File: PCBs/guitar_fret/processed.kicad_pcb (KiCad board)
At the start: 2 copper layers, 51 parts, among them J1 +5V, J10 CONN_01X06, J11 SWCLK, J2 GNDPWR, J3 +3.3V, J4 GND, J5 SDA, J6 SCL, J7 BOOT0, J8 NRST, J9 SWDIO, P0 TOUCH, P1 TOUCH, P2 TOUCH, P3 TOUCH, P4 TOUCH, P5 TOUCH, U1 STM32F051K*T, U2 AP2210N-3.3TRG1

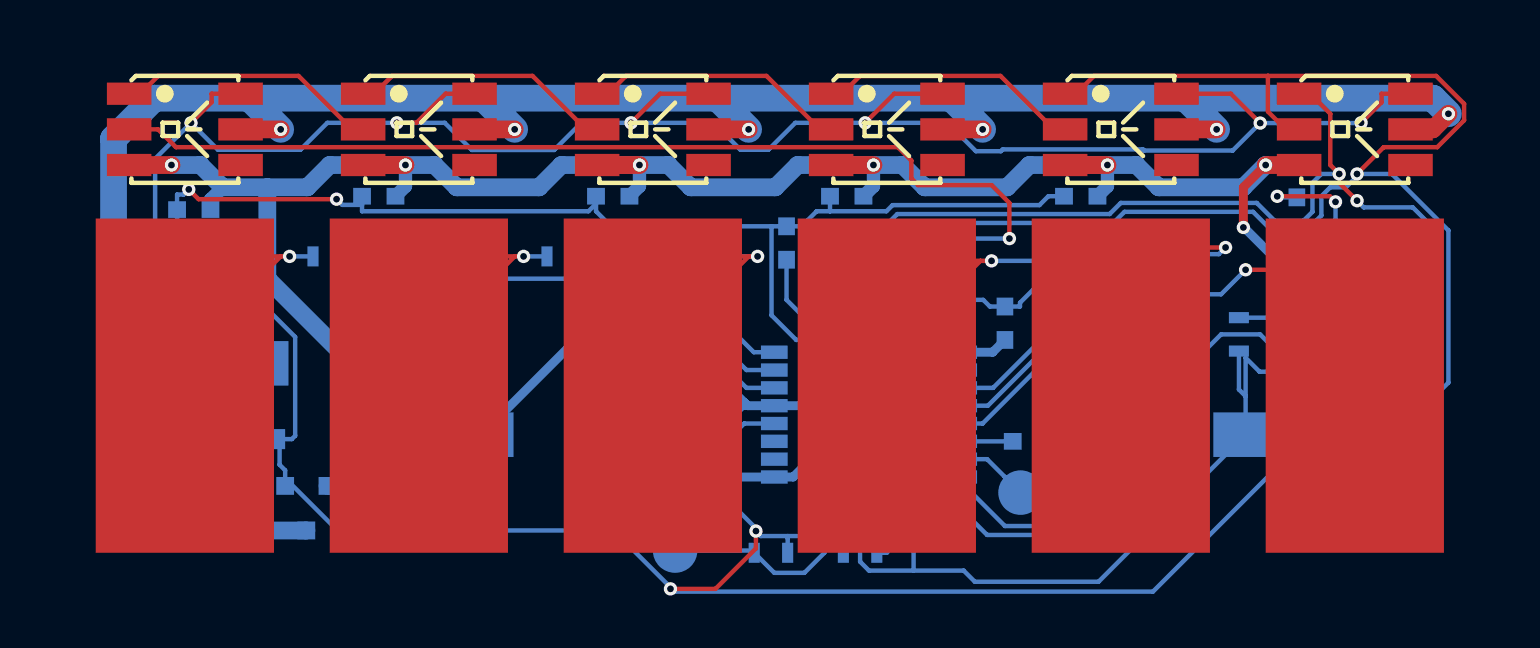
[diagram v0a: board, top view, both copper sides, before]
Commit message: debug boundaries of PCBs
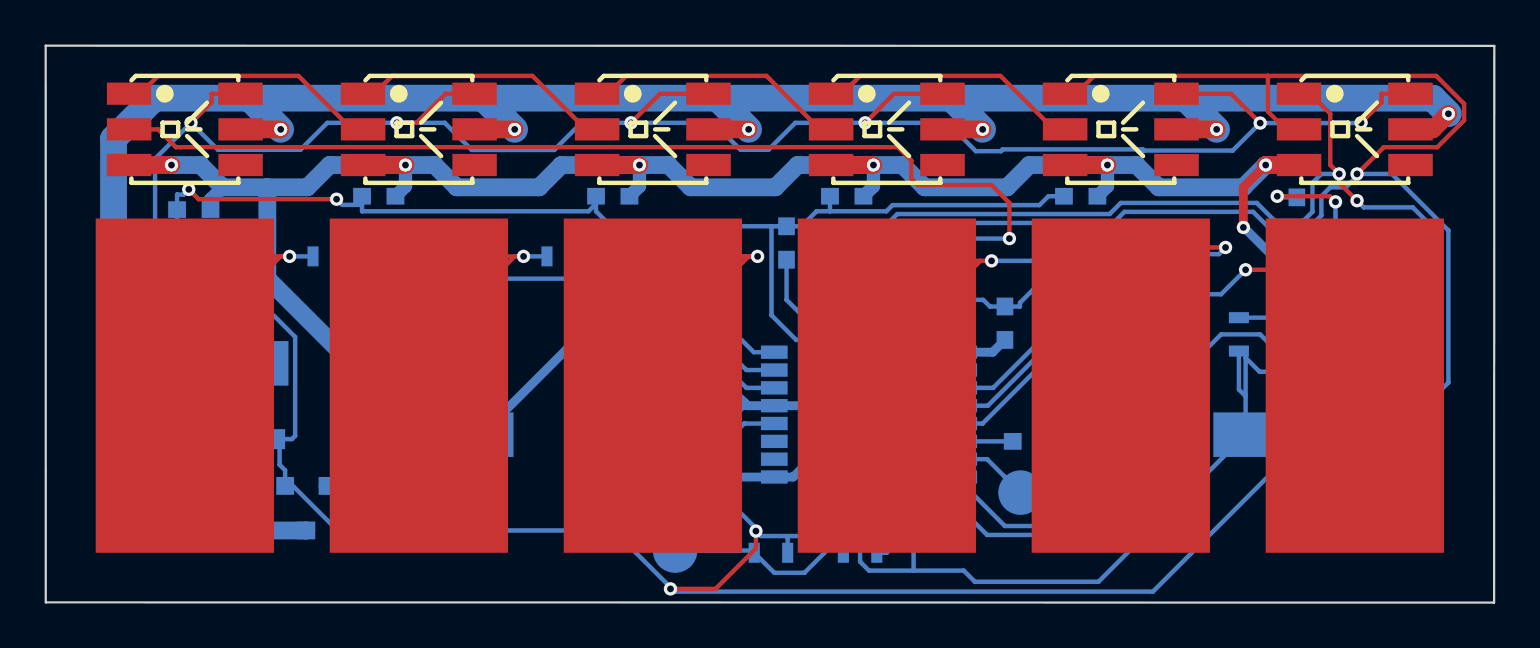
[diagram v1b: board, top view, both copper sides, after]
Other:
- board outline added: 65 x 25 mm
